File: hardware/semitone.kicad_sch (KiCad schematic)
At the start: 21 parts, among them SW1 SW_Rotary12, U5 OPA4991

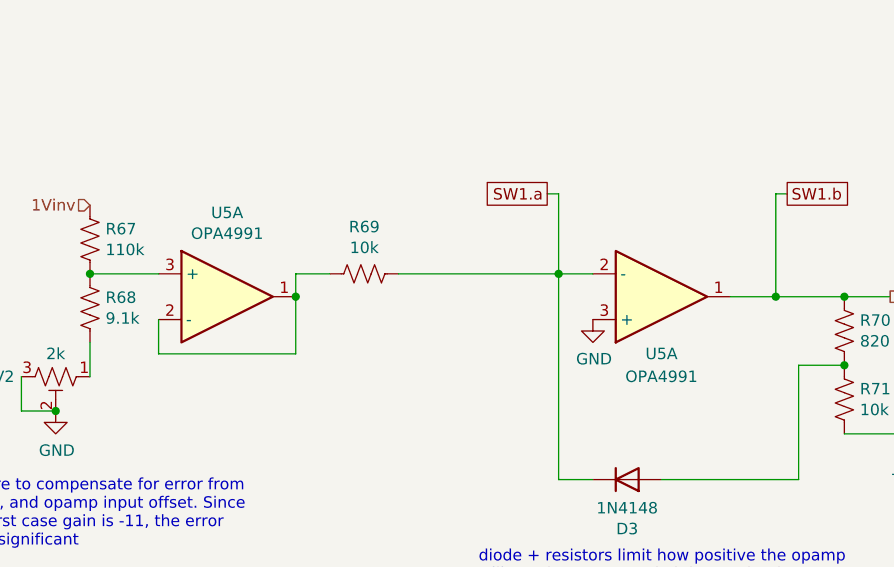
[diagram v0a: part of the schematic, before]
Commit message: Fix 3d models and migrate to KiCad6 R/C footprints
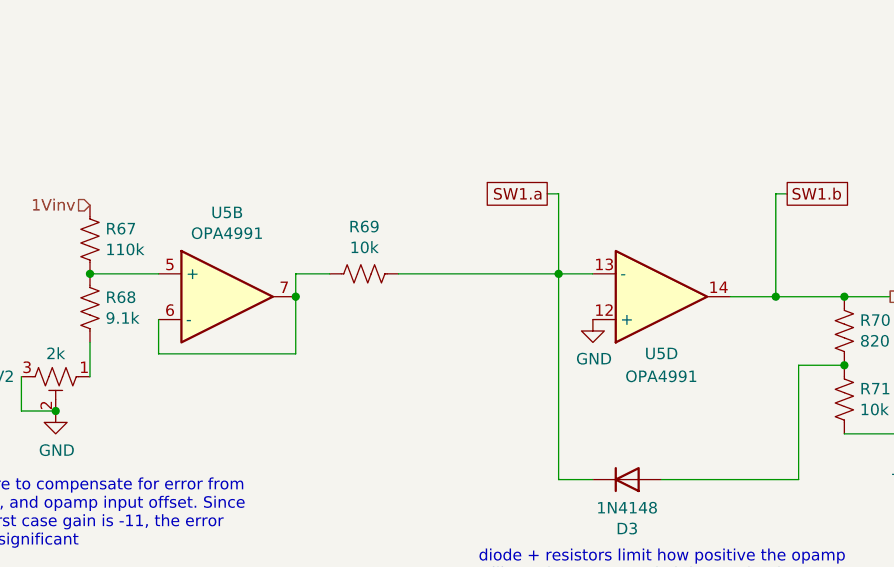
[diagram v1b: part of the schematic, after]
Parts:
- R67, R68, R69, R70, R71, R72, R73, R74, R75, R76, R77, R78, R79, R80, R81, R82: footprint Resistor_SMD:R_0603_1608Metric_Pad1.05x0.95mm_HandSolder -> Resistor_SMD:R_0603_1608Metric_Pad0.98x0.95mm_HandSolder
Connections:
- net GND: now also U5.12 (+); no longer U5.3 (+)
- net SW1.a: now also U5.13 (-); no longer U5.2 (-)
- net SW1.b: now also U5.14; no longer U5.1
- net at R67.1, R68.2: now also U5.5 (+); no longer U5.3 (+)
- new net: R69.2, U5.6 (-), U5.7
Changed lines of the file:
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@@
       (effects (font (size 1.27 1.27)) (justify left))
     )
-    (property "Footprint" "Resistor_SMD:R_0603_1608Metric_Pad1.05x0.95mm_HandSolder" (id 2) (at 135.636 131.064 90)
+    (property "Footprint" "Resistor_SMD:R_0603_1608Metric_Pad0.98x0.95mm_HandSolder" (id 2) (at 135.636 131.064 90)
       (effects (font (size 1.27 1.27)) hide)
     )
@@
       (effects (font (size 1.27 1.27)) (justify left))
     )
-    (property "Footprint" "Resistor_SMD:R_0603_1608Metric_Pad1.05x0.95mm_HandSolder" (id 2) (at 135.636 138.684 90)
+    (property "Footprint" "Resistor_SMD:R_0603_1608Metric_Pad0.98x0.95mm_HandSolder" (id 2) (at 135.636 138.684 90)
       (effects (font (size 1.27 1.27)) hide)
     )
@@
     (property "Reference" "R82" (id 0) (at 116.84 67.31 90))
     (property "Value" "10k" (id 1) (at 120.65 67.31 90))
-    (property "Footprint" "Resistor_SMD:R_0603_1608Metric_Pad1.05x0.95mm_HandSolder" (id 2) (at 110.744 66.294 90)
+    (property "Footprint" "Resistor_SMD:R_0603_1608Metric_Pad0.98x0.95mm_HandSolder" (id 2) (at 110.744 66.294 90)
       (effects (font (size 1.27 1.27)) hide)
     )
@@
     (property "Reference" "R81" (id 0) (at 116.84 64.77 90))
     (property "Value" "10k" (id 1) (at 120.65 64.77 90))
-    (property "Footprint" "Resistor_SMD:R_0603_1608Metric_Pad1.05x0.95mm_HandSolder" (id 2) (at 110.744 63.754 90)
+    (property "Footprint" "Resistor_SMD:R_0603_1608Metric_Pad0.98x0.95mm_HandSolder" (id 2) (at 110.744 63.754 90)
       (effects (font (size 1.27 1.27)) hide)
     )
@@
     (property "Reference" "R80" (id 0) (at 116.84 62.23 90))
     (property "Value" "10k" (id 1) (at 120.65 62.23 90))
-    (property "Footprint" "Resistor_SMD:R_0603_1608Metric_Pad1.05x0.95mm_HandSolder" (id 2) (at 110.744 61.214 90)
+    (property "Footprint" "Resistor_SMD:R_0603_1608Metric_Pad0.98x0.95mm_HandSolder" (id 2) (at 110.744 61.214 90)
       (effects (font (size 1.27 1.27)) hide)
     )
@@
     (property "Reference" "R79" (id 0) (at 116.84 59.69 90))
     (property "Value" "10k" (id 1) (at 120.65 59.69 90))
-    (property "Footprint" "Resistor_SMD:R_0603_1608Metric_Pad1.05x0.95mm_HandSolder" (id 2) (at 110.744 58.674 90)
+    (property "Footprint" "Resistor_SMD:R_0603_1608Metric_Pad0.98x0.95mm_HandSolder" (id 2) (at 110.744 58.674 90)
       (effects (font (size 1.27 1.27)) hide)
     )
@@
     (property "Reference" "R78" (id 0) (at 116.84 57.15 90))
     (property "Value" "10k" (id 1) (at 120.65 57.15 90))
-    (property "Footprint" "Resistor_SMD:R_0603_1608Metric_Pad1.05x0.95mm_HandSolder" (id 2) (at 110.744 56.134 90)
+    (property "Footprint" "Resistor_SMD:R_0603_1608Metric_Pad0.98x0.95mm_HandSolder" (id 2) (at 110.744 56.134 90)
       (effects (font (size 1.27 1.27)) hide)
     )
@@
     (property "Reference" "R77" (id 0) (at 116.84 52.07 90))
     (property "Value" "10k" (id 1) (at 120.65 52.07 90))
-    (property "Footprint" "Resistor_SMD:R_0603_1608Metric_Pad1.05x0.95mm_HandSolder" (id 2) (at 110.744 51.054 90)
+    (property "Footprint" "Resistor_SMD:R_0603_1608Metric_Pad0.98x0.95mm_HandSolder" (id 2) (at 110.744 51.054 90)
       (effects (font (size 1.27 1.27)) hide)
     )
@@
     (property "Reference" "R76" (id 0) (at 116.84 49.53 90))
     (property "Value" "10k" (id 1) (at 120.65 49.53 90))
-    (property "Footprint" "Resistor_SMD:R_0603_1608Metric_Pad1.05x0.95mm_HandSolder" (id 2) (at 110.744 48.514 90)
+    (property "Footprint" "Resistor_SMD:R_0603_1608Metric_Pad0.98x0.95mm_HandSolder" (id 2) (at 110.744 48.514 90)
       (effects (font (size 1.27 1.27)) hide)
     )
@@
     (property "Reference" "R75" (id 0) (at 116.84 46.99 90))
     (property "Value" "10k" (id 1) (at 120.65 46.99 90))
-    (property "Footprint" "Resistor_SMD:R_0603_1608Metric_Pad1.05x0.95mm_HandSolder" (id 2) (at 110.744 45.974 90)
+    (property "Footprint" "Resistor_SMD:R_0603_1608Metric_Pad0.98x0.95mm_HandSolder" (id 2) (at 110.744 45.974 90)
       (effects (font (size 1.27 1.27)) hide)
     )
@@
     (property "Reference" "R74" (id 0) (at 116.84 44.45 90))
     (property "Value" "10k" (id 1) (at 120.65 44.45 90))
-    (property "Footprint" "Resistor_SMD:R_0603_1608Metric_Pad1.05x0.95mm_HandSolder" (id 2) (at 110.744 43.434 90)
+    (property "Footprint" "Resistor_SMD:R_0603_1608Metric_Pad0.98x0.95mm_HandSolder" (id 2) (at 110.744 43.434 90)
       (effects (font (size 1.27 1.27)) hide)
     )
@@
     (property "Reference" "R73" (id 0) (at 116.84 41.91 90))
     (property "Value" "10k" (id 1) (at 120.65 41.91 90))
-    (property "Footprint" "Resistor_SMD:R_0603_1608Metric_Pad1.05x0.95mm_HandSolder" (id 2) (at 110.744 40.894 90)
+    (property "Footprint" "Resistor_SMD:R_0603_1608Metric_Pad0.98x0.95mm_HandSolder" (id 2) (at 110.744 40.894 90)
       (effects (font (size 1.27 1.27)) hide)
     )
@@
     (property "Reference" "R72" (id 0) (at 116.84 39.37 90))
     (property "Value" "10k" (id 1) (at 120.65 39.37 90))
-    (property "Footprint" "Resistor_SMD:R_0603_1608Metric_Pad1.05x0.95mm_HandSolder" (id 2) (at 110.744 38.354 90)
+    (property "Footprint" "Resistor_SMD:R_0603_1608Metric_Pad0.98x0.95mm_HandSolder" (id 2) (at 110.744 38.354 90)
       (effects (font (size 1.27 1.27)) hide)
     )
@@
     (pin "9")
   )
-  (symbol (lib_id "Device:Opamp_Quad_Generic") (at 114.3 127 0) (mirror x) (unit 1)
+  (symbol (lib_id "Device:Opamp_Quad_Generic") (at 114.3 127 0) (mirror x) (unit 4)
     (in_bom yes) (on_board yes)
     (property "Reference" "U5" (id 0) (at 114.3 133.35 0))
@@
       (effects (font (size 1.27 1.27)) hide)
     )
-    (pin "1")
-    (pin "2")
-    (pin "3")
+    (pin "12")
+    (pin "13")
+    (pin "14")
   )
   (symbol (lib_id "power:GND") (at 106.68 129.54 0) (unit 1)
@@
     (property "Reference" "R69" (id 0) (at 81.28 119.253 90))
     (property "Value" "10k" (id 1) (at 81.28 121.5644 90))
-    (property "Footprint" "Resistor_SMD:R_0603_1608Metric_Pad1.05x0.95mm_HandSolder" (id 2) (at 81.026 125.476 90)
+    (property "Footprint" "Resistor_SMD:R_0603_1608Metric_Pad0.98x0.95mm_HandSolder" (id 2) (at 81.026 125.476 90)
       (effects (font (size 1.27 1.27)) hide)
     )
@@
       (effects (font (size 1.27 1.27)) (justify right))
     )
-    (property "Footprint" "Resistor_SMD:R_0603_1608Metric_Pad1.05x0.95mm_HandSolder" (id 2) (at 49.784 120.396 90)
+    (property "Footprint" "Resistor_SMD:R_0603_1608Metric_Pad0.98x0.95mm_HandSolder" (id 2) (at 49.784 120.396 90)
       (effects (font (size 1.27 1.27)) hide)
     )
@@
       (effects (font (size 1.27 1.27)) (justify right))
     )
-    (property "Footprint" "Resistor_SMD:R_0603_1608Metric_Pad1.05x0.95mm_HandSolder" (id 2) (at 49.784 128.016 90)
+    (property "Footprint" "Resistor_SMD:R_0603_1608Metric_Pad0.98x0.95mm_HandSolder" (id 2) (at 49.784 128.016 90)
       (effects (font (size 1.27 1.27)) hide)
     )
@@
     (pin "1")
   )
-  (symbol (lib_id "Device:Opamp_Quad_Generic") (at 66.04 127 0) (unit 1)
+  (symbol (lib_id "Device:Opamp_Quad_Generic") (at 66.04 127 0) (unit 2)
     (in_bom yes) (on_board yes)
     (property "Reference" "U5" (id 0) (at 66.04 117.6782 0))
@@
       (effects (font (size 1.27 1.27)) hide)
     )
-    (pin "1")
-    (pin "2")
-    (pin "3")
+    (pin "5")
+    (pin "6")
+    (pin "7")
   )
 )
